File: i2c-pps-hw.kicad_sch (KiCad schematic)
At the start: 0 parts

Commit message: Create a page per devices block and connect them
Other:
- added sheet Controller and Power Stage (i2c-pps-hw-cps.kicad_sch)
- added sheet Digital IO and Indication (i2c-pps-hw-dio.kicad_sch)
- added sheet Input Filter and Sensor (i2c-pps-hw-input.kicad_sch)
- added sheet Master Switch (i2c-pps-hw-msw_sch.kicad_sch)
- added sheet Output Filter and Sensor (i2c-pps-hw-output.kicad_sch)
- added sheet Programming (i2c-pps-hw-prog.kicad_sch)

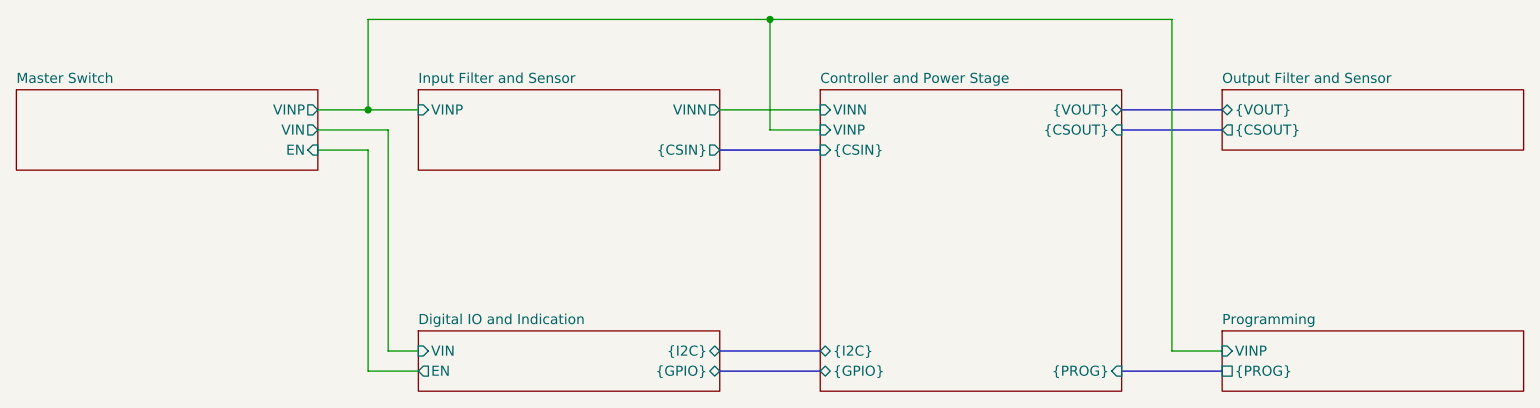
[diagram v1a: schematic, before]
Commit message: Design schematics and set per component requirements
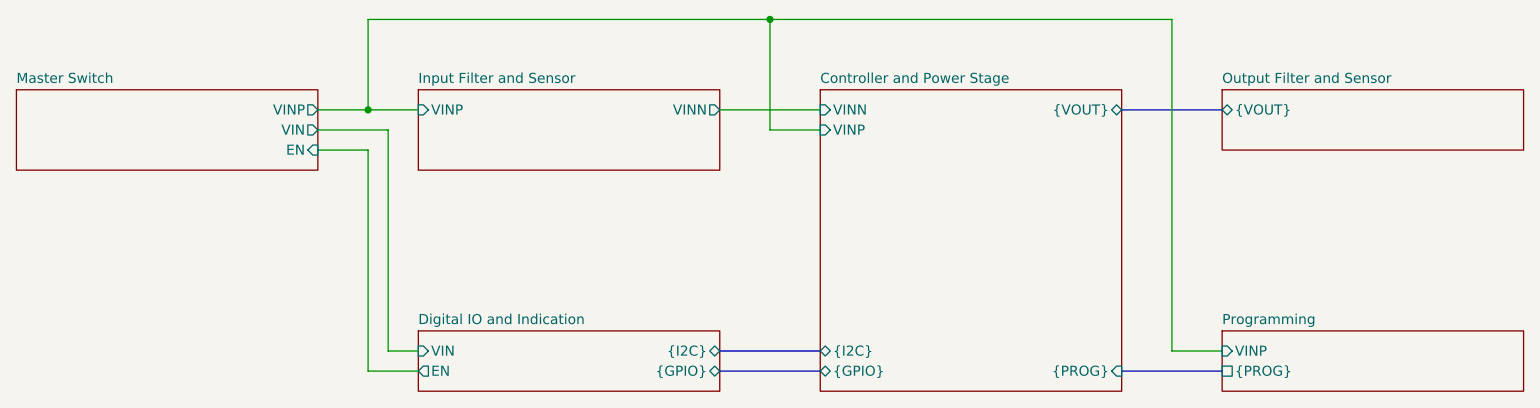
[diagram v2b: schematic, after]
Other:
- sheet Controller and Power Stage ports: added none; removed {CSIN}, {CSOUT}
- sheet Input Filter and Sensor ports: added none; removed {CSIN}
- sheet Output Filter and Sensor ports: added none; removed {CSOUT}
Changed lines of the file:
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@@
-		)
-	)
-	(bus
-		(pts
-			(xy 133.35 90.17) (xy 146.05 90.17)
-		)
-		(stroke
-			(width 0)
-			(type default)
 		)
 	)
@@
 		(pts
 			(xy 146.05 87.63) (xy 139.7 87.63)
-		)
-		(stroke
-			(width 0)
-			(type default)
-		)
-	)
-	(bus
-		(pts
-			(xy 184.15 87.63) (xy 196.85 87.63)
 		)
 		(stroke
@@
 			)
 		)
-		(pin "{CSOUT}" input
-			(at 184.15 87.63 0)
-			(effects
-				(font
-					(size 1.27 1.27)
-				)
-				(justify right)
-			)
-		)
 		(pin "VINN" input
 			(at 146.05 85.09 180)
-			(effects
-				(font
-					(size 1.27 1.27)
-				)
-				(justify left)
-			)
-		)
-		(pin "{CSIN}" input
-			(at 146.05 90.17 180)
 			(effects
 				(font
@@
 			)
 		)
-		(pin "{CSIN}" output
-			(at 133.35 90.17 0)
-			(effects
-				(font
-					(size 1.27 1.27)
-				)
-				(justify right)
-			)
-		)
 		(pin "VINN" output
 			(at 133.35 85.09 0)
@@
 			)
 		)
-		(pin "{CSOUT}" output
-			(at 196.85 87.63 180)
-			(effects
-				(font
-					(size 1.27 1.27)
-				)
-				(justify left)
-			)
-		)

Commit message: Rename VIN to +5V_Prot for clarity
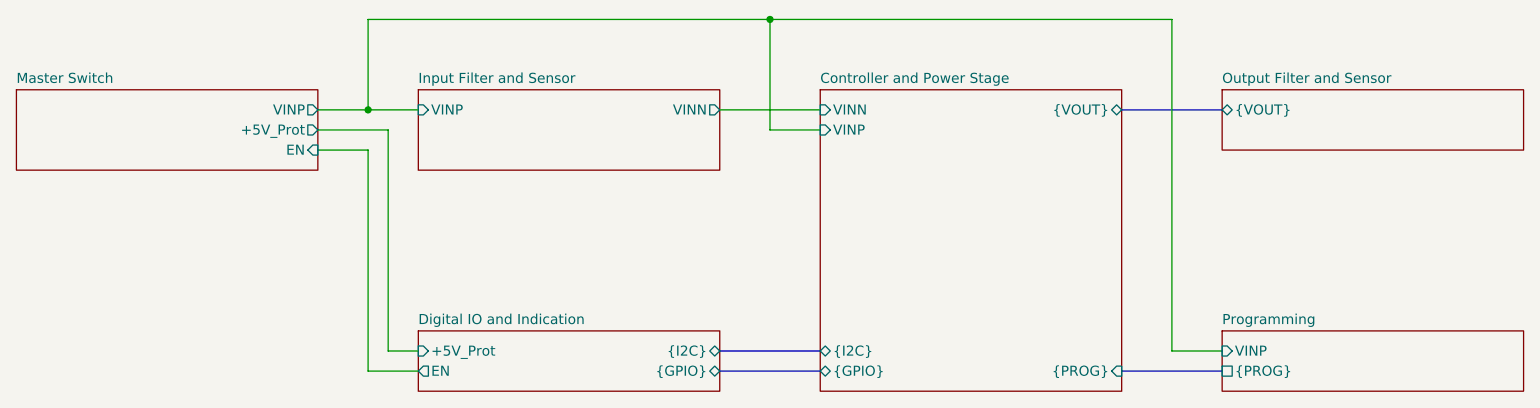
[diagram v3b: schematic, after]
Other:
- sheet Digital IO and Indication ports: added +5V_Prot; removed VIN
- sheet Master Switch ports: added +5V_Prot; removed VIN
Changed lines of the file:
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@@
 			)
 		)
-		(pin "VIN" output
+		(pin "+5V_Prot" output
 			(at 82.55 87.63 0)
 			(effects
@@
 			)
 		)
-		(pin "VIN" input
+		(pin "+5V_Prot" input
 			(at 95.25 115.57 180)
 			(effects

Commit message: Rename VINP to +5V_Run for clarity
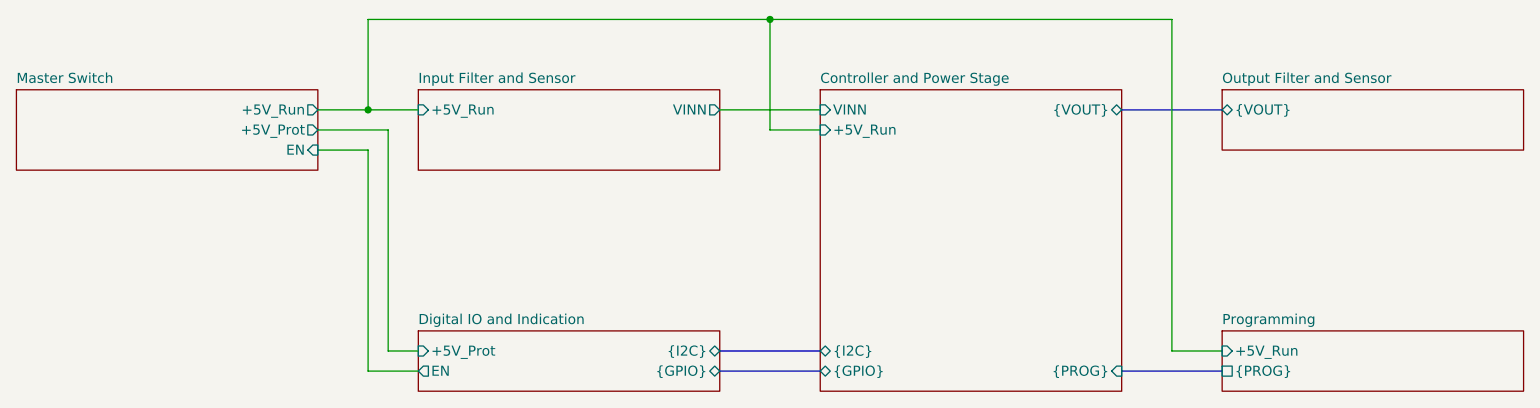
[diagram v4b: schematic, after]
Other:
- sheet Controller and Power Stage ports: added +5V_Run; removed VINP
- sheet Input Filter and Sensor ports: added +5V_Run; removed VINP
- sheet Master Switch ports: added +5V_Run; removed VINP
- sheet Programming ports: added +5V_Run; removed VINP
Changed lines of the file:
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@@
-			)
-		)
-		(pin "VINP" output
-			(at 82.55 85.09 0)
-			(effects
-				(font
-					(size 1.27 1.27)
-				)
-				(justify right)
 			)
 		)
@@
 		(pin "+5V_Prot" output
 			(at 82.55 87.63 0)
+			(effects
+				(font
+					(size 1.27 1.27)
+				)
+				(justify right)
+			)
+		)
+		(pin "+5V_Run" output
+			(at 82.55 85.09 0)
 			(effects
 				(font
@@
 			)
 		)
-		(pin "VINP" input
-			(at 146.05 87.63 180)
-			(effects
-				(font
-					(size 1.27 1.27)
-				)
-				(justify left)
-			)
-		)
 		(pin "{I2C}" bidirectional
 			(at 146.05 115.57 180)
@@
 				)
 				(justify right)
+			)
+		)
+		(pin "+5V_Run" input
+			(at 146.05 87.63 180)
+			(effects
+				(font
+					(size 1.27 1.27)
+				)
+				(justify left)
 			)
 		)
@@
 			)
 		)
-		(pin "VINP" input
+		(pin "+5V_Run" input
 			(at 196.85 115.57 180)
 			(effects
@@
 			)
 		)
-		(pin "VINP" input
-			(at 95.25 85.09 180)
-			(effects
-				(font
-					(size 1.27 1.27)
-				)
-				(justify left)
-			)
-		)
 		(pin "VINN" output
 			(at 133.35 85.09 0)
@@
 			)
 		)
+		(pin "+5V_Run" input
+			(at 95.25 85.09 180)
+			(effects
+				(font
+					(size 1.27 1.27)
+				)
+				(justify left)
+			)
+		)

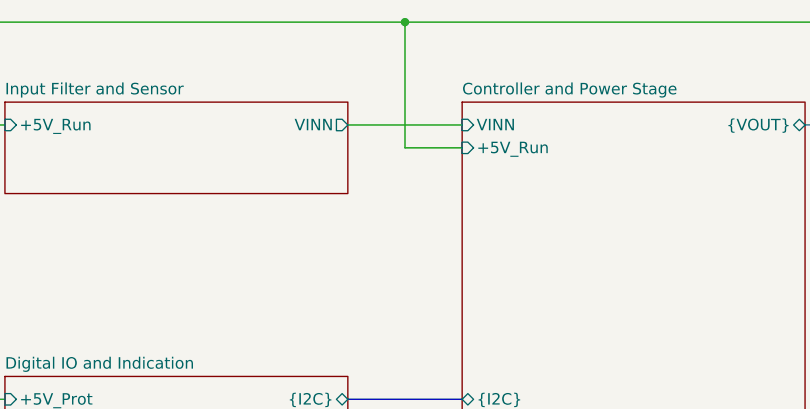
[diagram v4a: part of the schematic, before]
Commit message: Rename VINN to +5V_Filtered for clarity
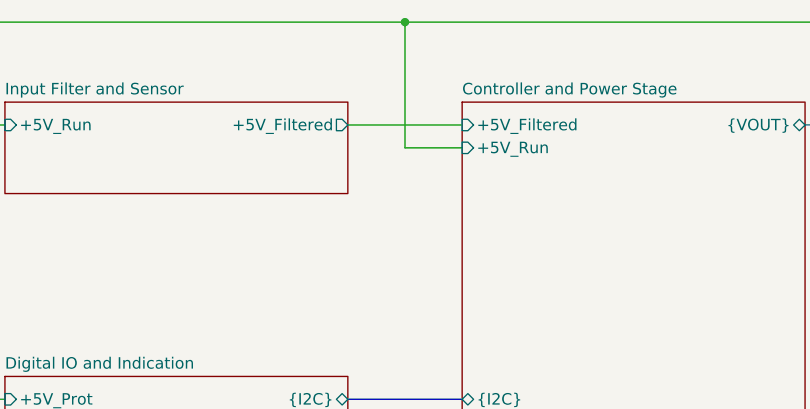
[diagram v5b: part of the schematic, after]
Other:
- sheet Controller and Power Stage ports: added +5V_Filtered; removed VINN
- sheet Input Filter and Sensor ports: added +5V_Filtered; removed VINN
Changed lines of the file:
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@@
-			)
-		)
-		(pin "VINN" input
-			(at 146.05 85.09 180)
-			(effects
-				(font
-					(size 1.27 1.27)
-				)
-				(justify left)
 			)
 		)
@@
 		(pin "+5V_Run" input
 			(at 146.05 87.63 180)
+			(effects
+				(font
+					(size 1.27 1.27)
+				)
+				(justify left)
+			)
+		)
+		(pin "+5V_Filtered" input
+			(at 146.05 85.09 180)
 			(effects
 				(font
@@
 			)
 		)
-		(pin "VINN" output
-			(at 133.35 85.09 0)
-			(effects
-				(font
-					(size 1.27 1.27)
-				)
-				(justify right)
-			)
-		)
 		(pin "+5V_Run" input
 			(at 95.25 85.09 180)
@@
 			)
 		)
+		(pin "+5V_Filtered" output
+			(at 133.35 85.09 0)
+			(effects
+				(font
+					(size 1.27 1.27)
+				)
+				(justify right)
+			)
+		)

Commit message: Select market available components
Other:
- sheet Master Switch: file i2c-pps-hw-msw_sch.kicad_sch -> i2c-pps-hw-msw.kicad_sch
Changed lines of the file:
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@@
 			)
 		)
-		(property "Sheetfile" "i2c-pps-hw-msw_sch.kicad_sch"
+		(property "Sheetfile" "i2c-pps-hw-msw.kicad_sch"
 			(at 44.45 93.2946 0)
 			(effects
